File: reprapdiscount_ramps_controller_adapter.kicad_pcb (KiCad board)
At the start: 2 copper layers, 62.1 x 21.2 mm, 7 parts

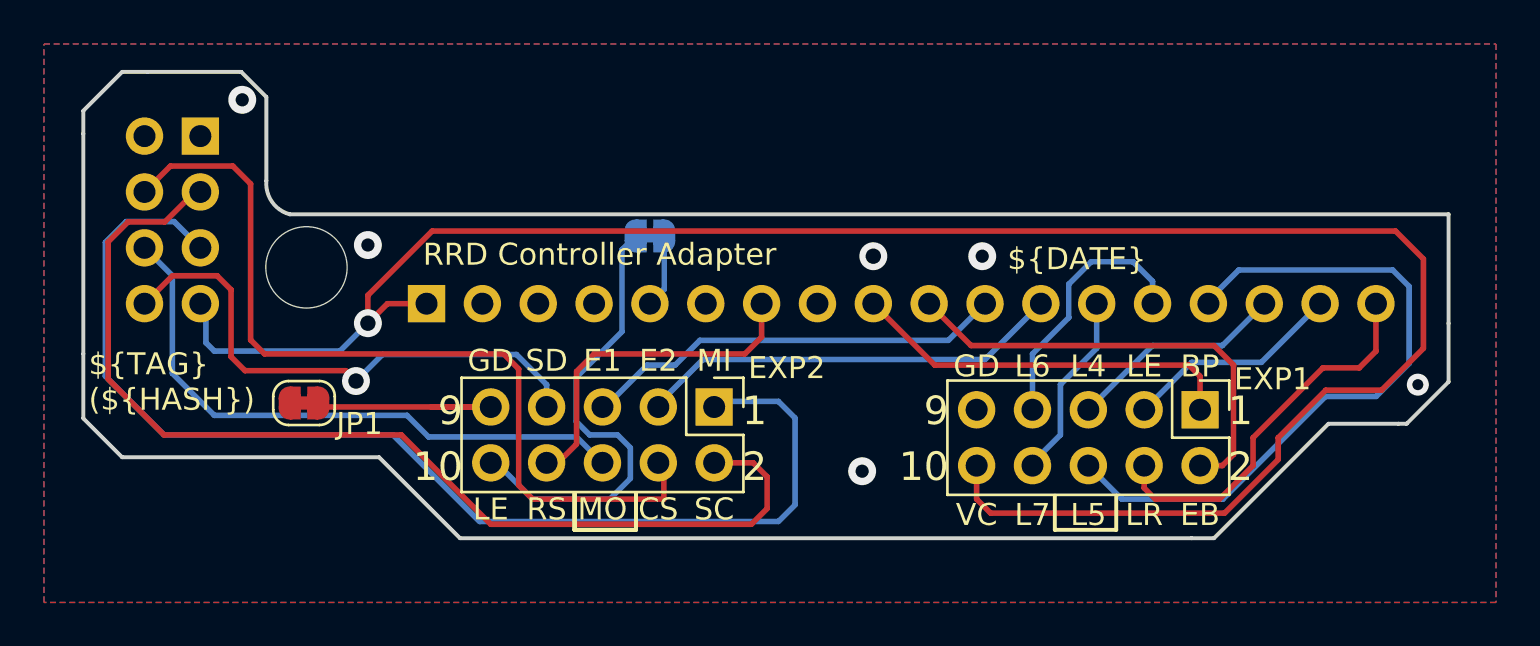
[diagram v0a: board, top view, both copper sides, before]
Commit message: adapter: minor track adjustments
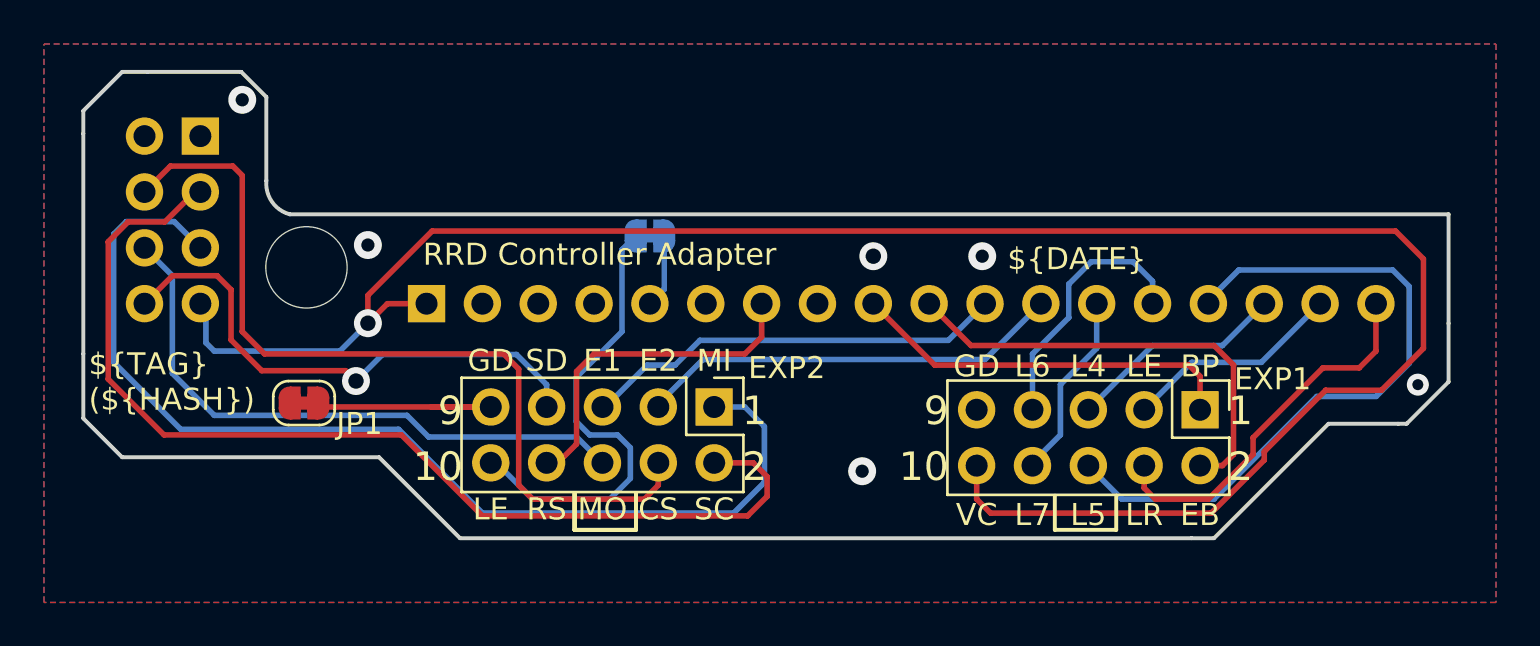
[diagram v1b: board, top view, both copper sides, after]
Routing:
- net SD_MISO: track 53.8 -> 48.7 mm
- net HOST_CS: track 39.4 -> 38.7 mm
- net HOST_SCK: track 48.5 -> 47.9 mm
